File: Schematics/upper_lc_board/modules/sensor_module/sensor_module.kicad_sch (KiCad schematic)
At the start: 20 parts, among them J5 HALL, U7 ADC_ADS131M04IPWR

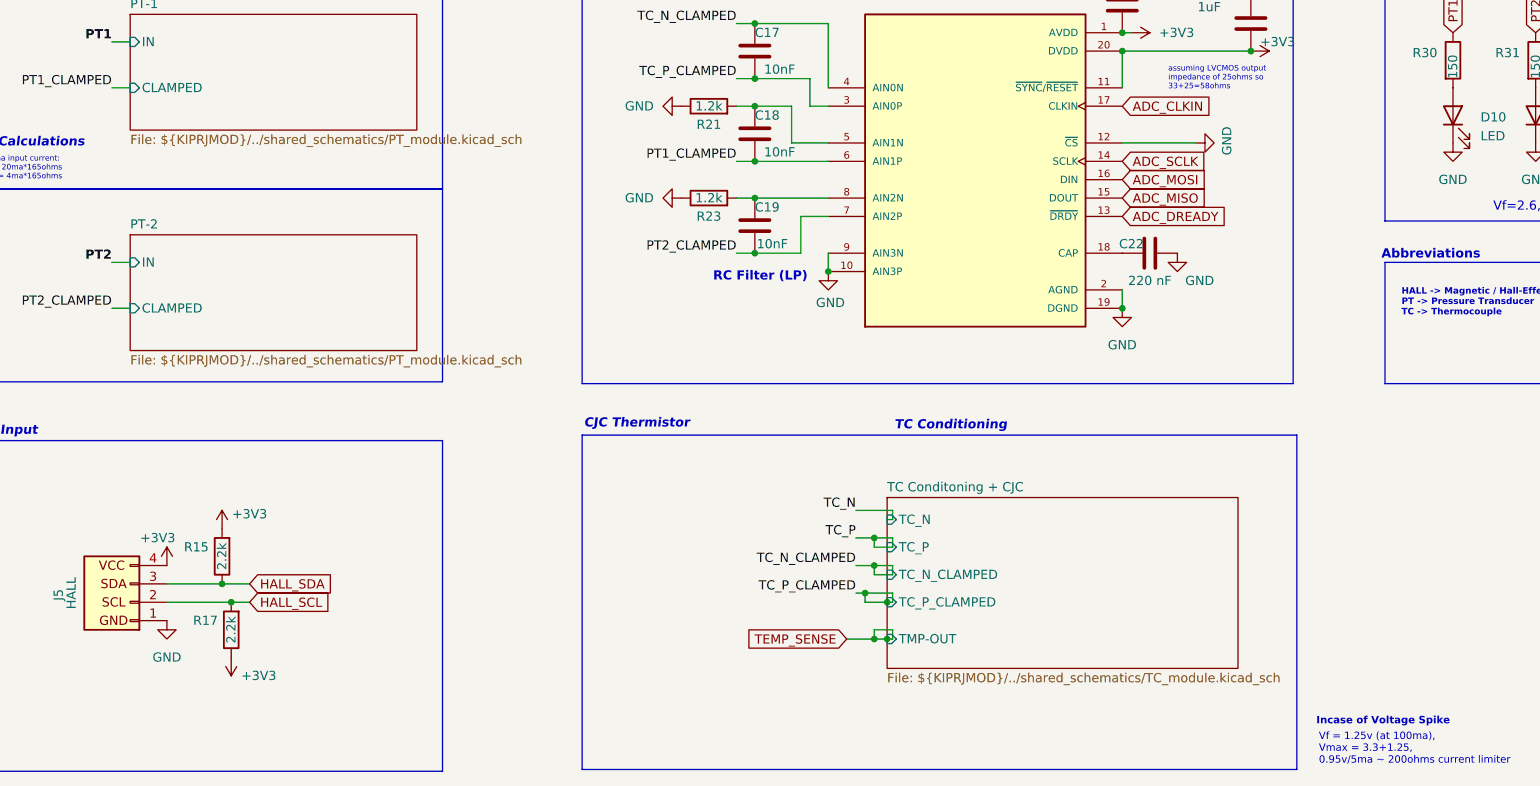
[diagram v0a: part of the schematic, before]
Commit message: fixed TC, PT, Valve schematic references and confirmed by updating PCB
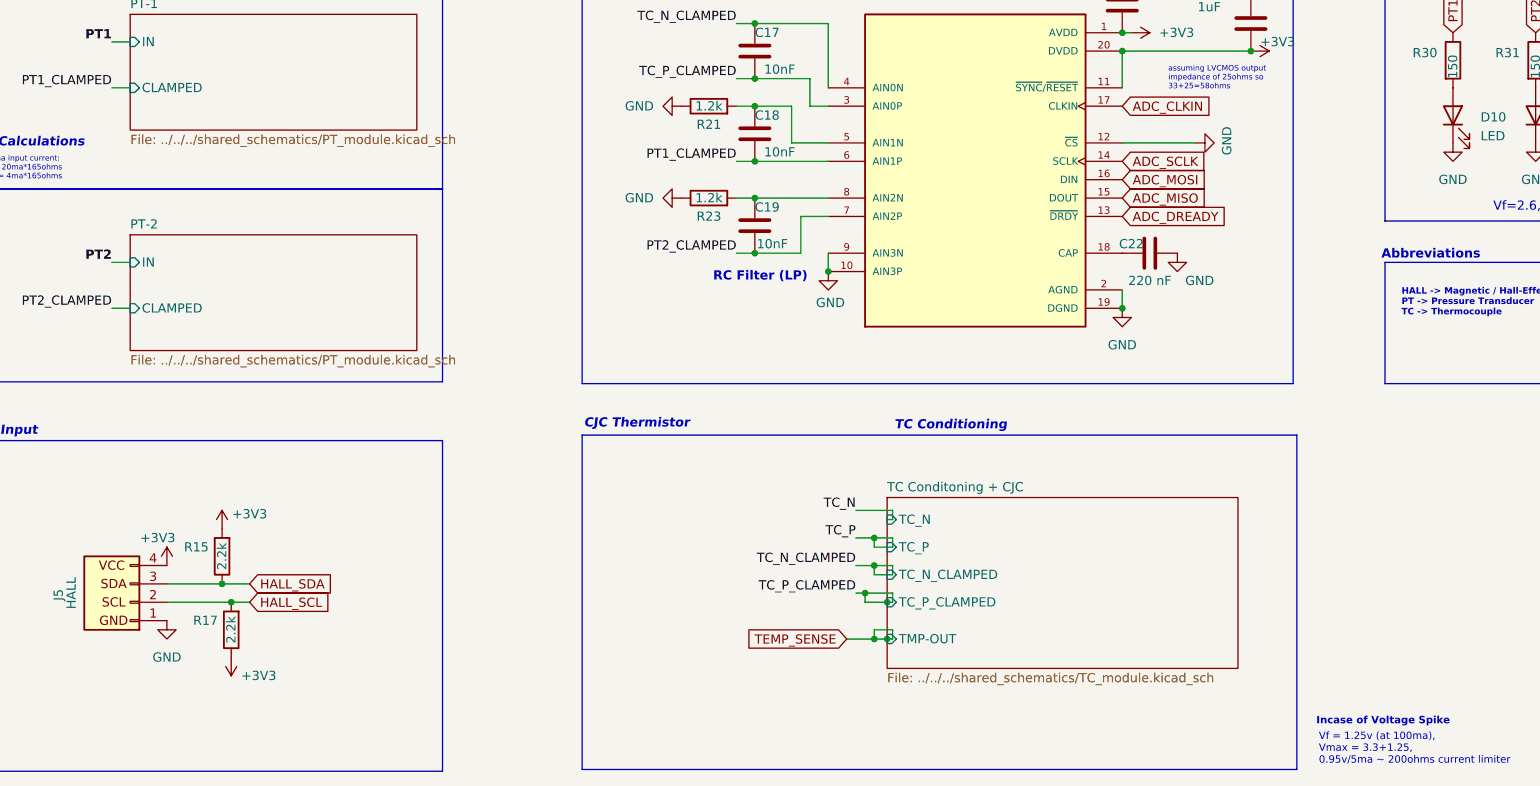
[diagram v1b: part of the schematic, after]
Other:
- sheet PT-1: file ${KIPRJMOD}/../shared_schematics/PT_module.kicad_sch -> ../../../shared_schematics/PT_module.kicad_sch
- sheet PT-2: file ${KIPRJMOD}/../shared_schematics/PT_module.kicad_sch -> ../../../shared_schematics/PT_module.kicad_sch
- sheet TC Conditoning + CJC: file ${KIPRJMOD}/../shared_schematics/TC_module.kicad_sch -> ../../../shared_schematics/TC_module.kicad_sch
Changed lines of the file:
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@@
 			)
 		)
-		(property "Sheetfile" "${KIPRJMOD}/../shared_schematics/PT_module.kicad_sch"
+		(property "Sheetfile" "../../../shared_schematics/PT_module.kicad_sch"
 			(at 46.99 63.5766 0)
 			(effects
@@
 			)
 		)
-		(property "Sheetfile" "${KIPRJMOD}/../shared_schematics/PT_module.kicad_sch"
+		(property "Sheetfile" "../../../shared_schematics/PT_module.kicad_sch"
 			(at 46.99 94.0566 0)
 			(effects
@@
 			)
 		)
-		(property "Sheetfile" "${KIPRJMOD}/../shared_schematics/TC_module.kicad_sch"
+		(property "Sheetfile" "../../../shared_schematics/TC_module.kicad_sch"
 			(at 151.638 137.9986 0)
 			(effects

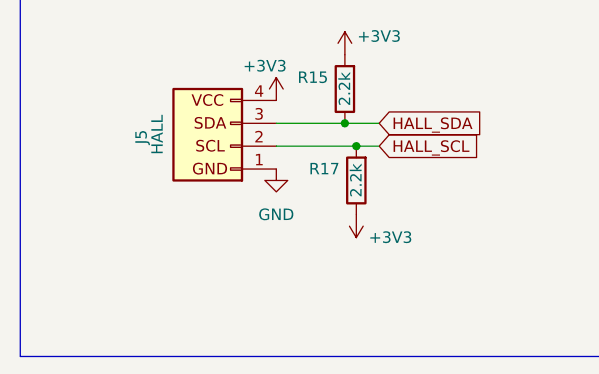
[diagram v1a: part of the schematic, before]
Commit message: add decoupling, revise power circuitry (ferrite bead, LDO swap), merge shared-schemtic branch changes.
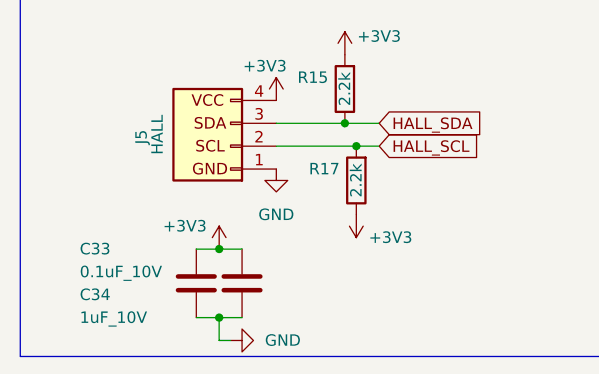
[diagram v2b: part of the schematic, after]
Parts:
- added C33: 0.1uF_10V, Capacitor_SMD:C_0805_2012Metric, symbol Device:C
- added C34: 1uF_10V, Capacitor_SMD:C_1206_3216Metric, symbol Device:C
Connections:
- net +3V3: now also C33.1, C34.1
- net GND: now also C33.2, C34.2
